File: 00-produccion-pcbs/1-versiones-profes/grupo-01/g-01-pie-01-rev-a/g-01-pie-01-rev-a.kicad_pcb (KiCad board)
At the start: 2 copper layers, 94.6 x 75.6 mm, 52 parts, among them J2 Conn_01x02_Pin, J4 Barrel_Jack_Switch, J5 Barrel_Jack_Switch, J6 AudioJack2_SwitchT, J7 Conn_01x03_Pin, J8 AudioJack2_SwitchT, J9 AudioJack2_SwitchT, Q1 2N2222, SW3 SW_SPDT, U1 NE555P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

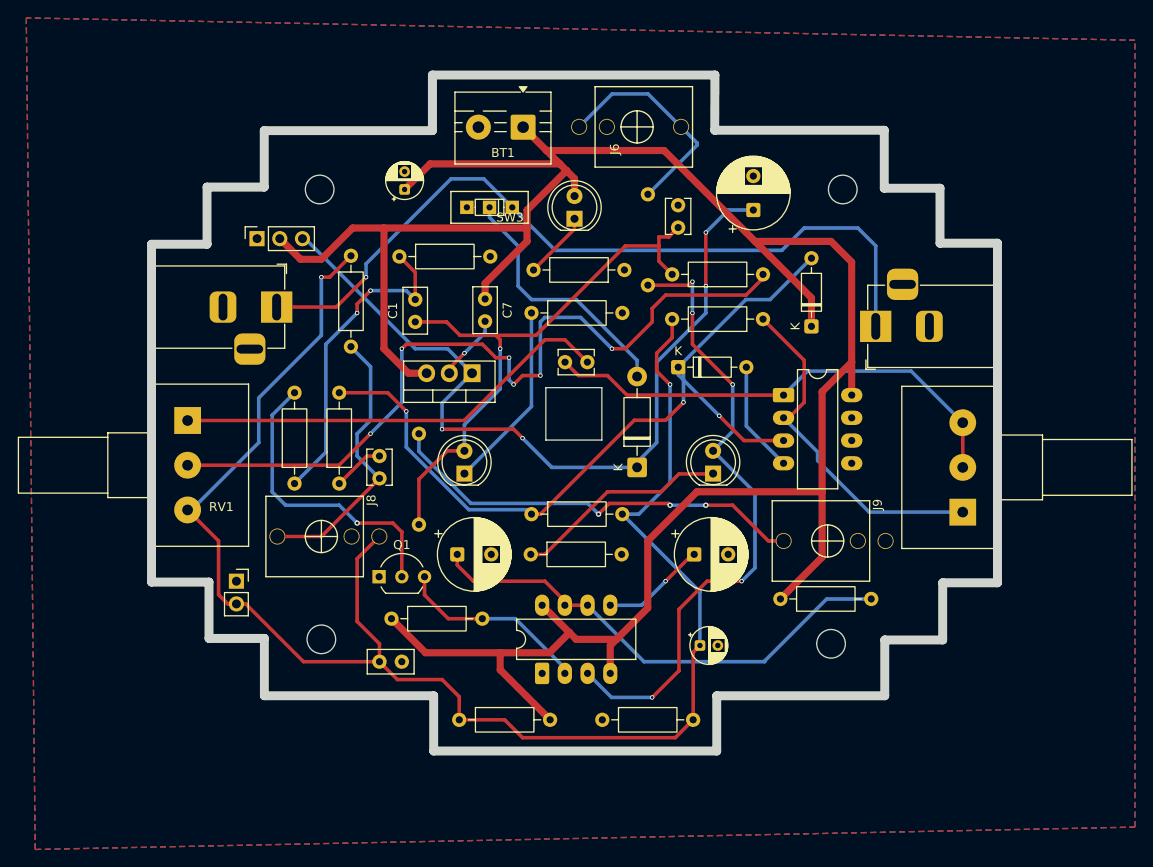
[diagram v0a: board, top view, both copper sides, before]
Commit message: corregido g01
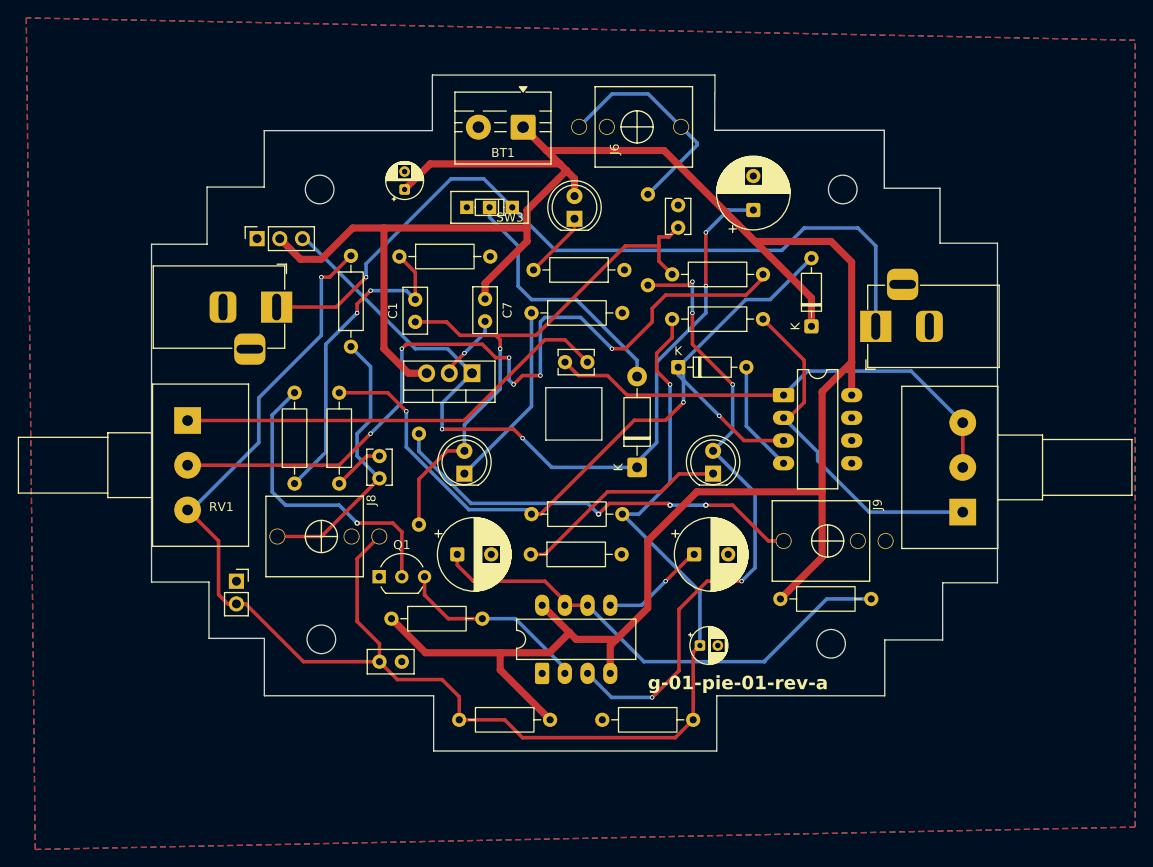
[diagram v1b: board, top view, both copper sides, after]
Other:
- board text added: "g-01-pie-01-rev-a"
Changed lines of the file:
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@@
 		)
 		(stroke
-			(width 1)
+			(width 0.1)
 			(type solid)
 			(color 0 79 255 1)
@@
 		(layer "User.1")
 	)
+	(gr_text "g-01-pie-01-rev-a"
+		(at 154.5 131.758582 0)
+		(layer "F.SilkS")
+		(effects
+			(font
+				(size 1.5 1.5)
+				(thickness 0.3)
+				(bold yes)
+			)
+			(justify left bottom)
+		)
+	)
 	(segment
 		(start 146.31 80.11)
@@
 	)
 	(segment
+		(start 113.08 114.5)
+		(end 118 114.5)
+		(width 0.4)
+		(layer "F.Cu")
+		(net "Net-(C9-Pad1)")
+	)
+	(segment
+		(start 118 114.5)
+		(end 124.5 108)
+		(width 0.4)
+		(layer "F.Cu")
+		(net "Net-(C9-Pad1)")
+	)
+	(segment
+		(start 123.5 101.5)
+		(end 122 103)
+		(width 0.4)
+		(layer "B.Cu")
+		(net "Net-(C9-Pad1)")
+	)
+	(segment
+		(start 122 103)
+		(end 122 105.5)
+		(width 0.4)
+		(layer "B.Cu")
+		(net "Net-(C9-Pad1)")
+	)
+	(segment
+		(start 121.31 93.27)
+		(end 121.31 93.31)
+		(width 0.4)
+		(layer "B.Cu")
+		(net "Net-(C9-Pad1)")
+	)
+	(segment
+		(start 121.31 93.31)
+		(end 123.5 95.5)
+		(width 0.4)
+		(layer "B.Cu")
+		(net "Net-(C9-Pad1)")
+	)
+	(segment
+		(start 122 105.5)
+		(end 124.5 108)
+		(width 0.4)
+		(layer "B.Cu")
+		(net "Net-(C9-Pad1)")
+	)
+	(segment
+		(start 123.5 95.5)
+		(end 123.5 101.5)
+		(width 0.4)
+		(layer "B.Cu")
+		(net "Net-(C9-Pad1)")
+	)
+	(segment
 		(start 124.5 105.5)
 		(end 123.08 105.5)
@@
 	)
 	(segment
+		(start 146.83 68.69)
+		(end 146.83 68.17)
+		(width 0.4)
+		(layer "F.Cu")
+		(net "Net-(J6-Pad1)")
+	)
+	(segment
+		(start 150.52 65)
+		(end 146.83 68.69)
+		(width 0.4)
+		(layer "B.Cu")
+		(net "Net-(J6-Pad1)")
+	)
+	(segment
+		(start 158.23 68.69)
+		(end 154.54 65)
+		(width 0.4)
+		(layer "B.Cu")
+		(net "Net-(J6-Pad1)")
+	)
+	(segment
+		(start 158.23 68.69)
+		(end 160 70.46)
+		(width 0.4)
+		(layer "B.Cu")
+		(net "Net-(J6-Pad1)")
+	)
+	(segment
+		(start 154.518466 76.235925)
+		(end 160 70.754391)
+		(width 0.4)
+		(layer "B.Cu")
+		(net "Net-(J6-Pad1)")
+	)
+	(segment
+		(start 160 70.754391)
+		(end 160 70.46)
+		(width 0.4)
+		(layer "B.Cu")
+		(net "Net-(J6-Pad1)")
+	)
+	(segment
+		(start 154.54 65)
+		(end 150.52 65)
+		(width 0.4)
+		(layer "B.Cu")
+		(net "Net-(J6-Pad1)")
+	)
+	(segment
 		(start 122 89.5)
 		(end 122 88.5)
@@
 	)
 	(segment
+		(start 169.7 115)
+		(end 168 115)
+		(width 0.4)
+		(layer "F.Cu")
+		(net "Net-(J9-Pad3)")
+	)
+	(segment
+		(start 168 115)
+		(end 164 111)
+		(width 0.4)
+		(layer "F.Cu")
+		(net "Net-(J9-Pad3)")
+	)
+	(segment
+		(start 164 111)
+		(end 161 111)
+		(width 0.4)
+		(layer "F.Cu")
+		(net "Net-(J9-Pad3)")
+	)
+	(segment
+		(start 150.2 110.8)
+		(end 149 112)
+		(width 0.4)
+		(layer "F.Cu")
+		(net "Net-(J9-Pad3)")
+	)
+	(segment
+		(start 157 111)
+		(end 156.8 110.8)
+		(width 0.4)
+		(layer "F.Cu")
+		(net "Net-(J9-Pad3)")
+	)
+	(segment
+		(start 156.8 110.8)
+		(end 150.2 110.8)
+		(width 0.4)
+		(layer "F.Cu")
+		(net "Net-(J9-Pad3)")
+	)
+	(via
+		(at 149 112)
+		(size 0.6)
+		(drill 0.3)
+		(layers "F.Cu" "B.Cu")
+		(net "Net-(J9-Pad3)")
+	)
+	(via
+		(at 161 111)
+		(size 0.6)
+		(drill 0.3)
+		(layers "F.Cu" "B.Cu")
+		(net "Net-(J9-Pad3)")
+	)
+	(via
+		(at 157 111)
+		(size 0.6)
+		(drill 0.3)
+		(layers "F.Cu" "B.Cu")
+		(net "Net-(J9-Pad3)")
+	)
+	(segment
+		(start 134.735 110.8)
+		(end 128.911616 104.976616)
+		(width 0.4)
+		(layer "B.Cu")
+		(net "Net-(J9-Pad3)")
+	)
+	(segment
+		(start 128.911616 104.976616)
+		(end 128.911616 103.008126)
+		(width 0.4)
+		(layer "B.Cu")
+		(net "Net-(J9-Pad3)")
+	)
+	(segment
+		(start 149 112)
+		(end 147.8 110.8)
+		(width 0.4)
+		(layer "B.Cu")
+		(net "Net-(J9-Pad3)")
+	)
+	(segment
+		(start 147.8 110.8)
+		(end 134.735 110.8)
+		(width 0.4)
+		(layer "B.Cu")
+		(net "Net-(J9-Pad3)")
+	)
+	(segment
+		(start 161 111)
+		(end 157 111)
+		(width 0.4)
+		(layer "B.Cu")
+		(net "Net-(J9-Pad3)")
+	)
+	(segment
 		(start 119.655679 88.844321)
 		(end 113 88.844321)
@@
 		(layer "F.Cu")
 		(net "Net-(D2-K)")
-	)
-	(segment
-		(start 113.08 114.5)
-		(end 118 114.5)
-		(width 0.4)
-		(layer "F.Cu")
-		(net "Net-(C9-Pad1)")
-	)
-	(segment
-		(start 118 114.5)
-		(end 124.5 108)
-		(width 0.4)
-		(layer "F.Cu")
-		(net "Net-(C9-Pad1)")
-	)
-	(segment
-		(start 123.5 101.5)
-		(end 122 103)
-		(width 0.4)
-		(layer "B.Cu")
-		(net "Net-(C9-Pad1)")
-	)
-	(segment
-		(start 122 103)
-		(end 122 105.5)
-		(width 0.4)
-		(layer "B.Cu")
-		(net "Net-(C9-Pad1)")
-	)
-	(segment
-		(start 121.31 93.27)
-		(end 121.31 93.31)
-		(width 0.4)
-		(layer "B.Cu")
-		(net "Net-(C9-Pad1)")
-	)
-	(segment
-		(start 121.31 93.31)
-		(end 123.5 95.5)
-		(width 0.4)
-		(layer "B.Cu")
-		(net "Net-(C9-Pad1)")
-	)
-	(segment
-		(start 122 105.5)
-		(end 124.5 108)
-		(width 0.4)
-		(layer "B.Cu")
-		(net "Net-(C9-Pad1)")
-	)
-	(segment
-		(start 123.5 95.5)
-		(end 123.5 101.5)
-		(width 0.4)
-		(layer "B.Cu")
-		(net "Net-(C9-Pad1)")
-	)
-	(segment
-		(start 146.83 68.69)
-		(end 146.83 68.17)
-		(width 0.4)
-		(layer "F.Cu")
-		(net "Net-(J6-Pad1)")
-	)
-	(segment
-		(start 150.52 65)
-		(end 146.83 68.69)
-		(width 0.4)
-		(layer "B.Cu")
-		(net "Net-(J6-Pad1)")
-	)
-	(segment
-		(start 158.23 68.69)
-		(end 154.54 65)
-		(width 0.4)
-		(layer "B.Cu")
-		(net "Net-(J6-Pad1)")
-	)
-	(segment
-		(start 158.23 68.69)
-		(end 160 70.46)
-		(width 0.4)
-		(layer "B.Cu")
-		(net "Net-(J6-Pad1)")
-	)
-	(segment
-		(start 154.518466 76.235925)
-		(end 160 70.754391)
-		(width 0.4)
-		(layer "B.Cu")
-		(net "Net-(J6-Pad1)")
-	)
-	(segment
-		(start 160 70.754391)
-		(end 160 70.46)
-		(width 0.4)
-		(layer "B.Cu")
-		(net "Net-(J6-Pad1)")
-	)
-	(segment
-		(start 154.54 65)
-		(end 150.52 65)
-		(width 0.4)
-		(layer "B.Cu")
-		(net "Net-(J6-Pad1)")
-	)
-	(segment
-		(start 169.7 115)
-		(end 168 115)
-		(width 0.4)
-		(layer "F.Cu")
-		(net "Net-(J9-Pad3)")
-	)
-	(segment
-		(start 168 115)
-		(end 164 111)
-		(width 0.4)
-		(layer "F.Cu")
-		(net "Net-(J9-Pad3)")
-	)
-	(segment
-		(start 164 111)
-		(end 161 111)
-		(width 0.4)
-		(layer "F.Cu")
-		(net "Net-(J9-Pad3)")
-	)
-	(segment
-		(start 150.2 110.8)
-		(end 149 112)
-		(width 0.4)
-		(layer "F.Cu")
-		(net "Net-(J9-Pad3)")
-	)
-	(segment
-		(start 157 111)
-		(end 156.8 110.8)
-		(width 0.4)
-		(layer "F.Cu")
-		(net "Net-(J9-Pad3)")
-	)
-	(segment
-		(start 156.8 110.8)
-		(end 150.2 110.8)
-		(width 0.4)
-		(layer "F.Cu")
-		(net "Net-(J9-Pad3)")
-	)
-	(via
-		(at 149 112)
-		(size 0.6)
-		(drill 0.3)
-		(layers "F.Cu" "B.Cu")
-		(net "Net-(J9-Pad3)")
-	)
-	(via
-		(at 161 111)
-		(size 0.6)
-		(drill 0.3)
-		(layers "F.Cu" "B.Cu")
-		(net "Net-(J9-Pad3)")
-	)
-	(via
-		(at 157 111)
-		(size 0.6)
-		(drill 0.3)
-		(layers "F.Cu" "B.Cu")
-		(net "Net-(J9-Pad3)")
-	)
-	(segment
-		(start 134.735 110.8)
-		(end 128.911616 104.976616)
-		(width 0.4)
-		(layer "B.Cu")
-		(net "Net-(J9-Pad3)")
-	)
-	(segment
-		(start 128.911616 104.976616)
-		(end 128.911616 103.008126)
-		(width 0.4)
-		(layer "B.Cu")
-		(net "Net-(J9-Pad3)")
-	)
-	(segment
-		(start 149 112)
-		(end 147.8 110.8)
-		(width 0.4)
-		(layer "B.Cu")
-		(net "Net-(J9-Pad3)")
-	)
-	(segment
-		(start 147.8 110.8)
-		(end 134.735 110.8)
-		(width 0.4)
-		(layer "B.Cu")
-		(net "Net-(J9-Pad3)")
-	)
-	(segment
-		(start 161 111)
-		(end 157 111)
-		(width 0.4)
-		(layer "B.Cu")
-		(net "Net-(J9-Pad3)")
 	)
 	(zone
@@
 	)
 	(group ""
-		(members "59cb93a7-08dd-4761-9e52-da9c0941d633" "e6252792-57c9-454e-ac68-b061a26b515c")
-	)
-	(group ""
